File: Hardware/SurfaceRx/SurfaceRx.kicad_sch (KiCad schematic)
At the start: 26 parts

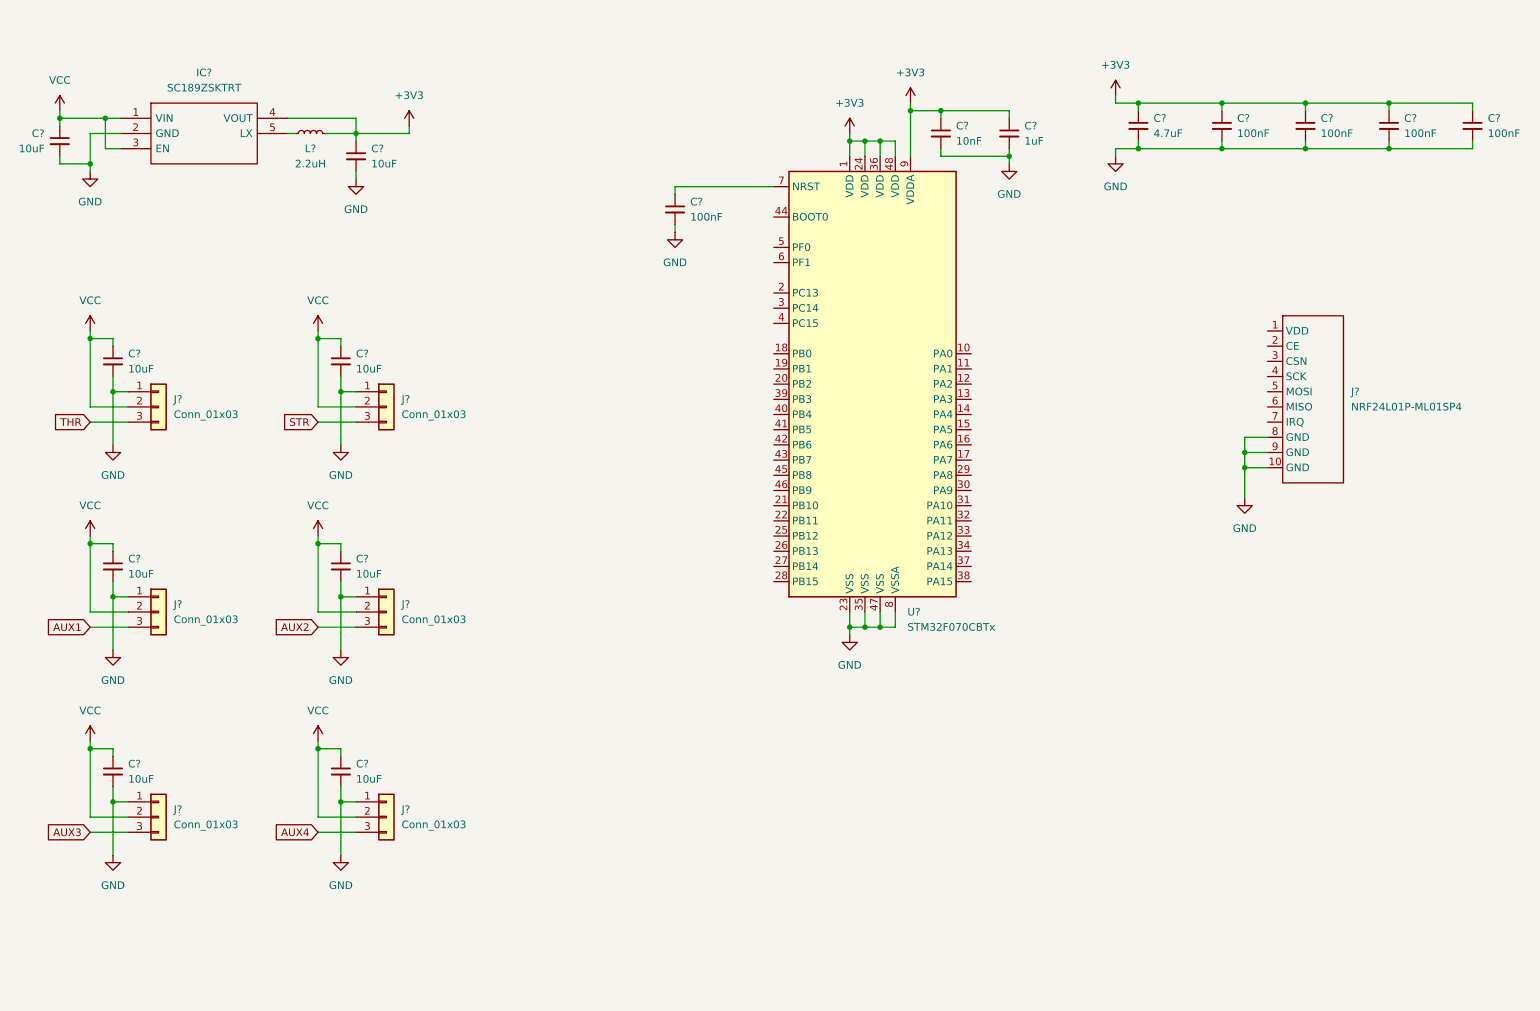
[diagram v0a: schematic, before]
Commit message: changed microcontroller to STM32G070KBT
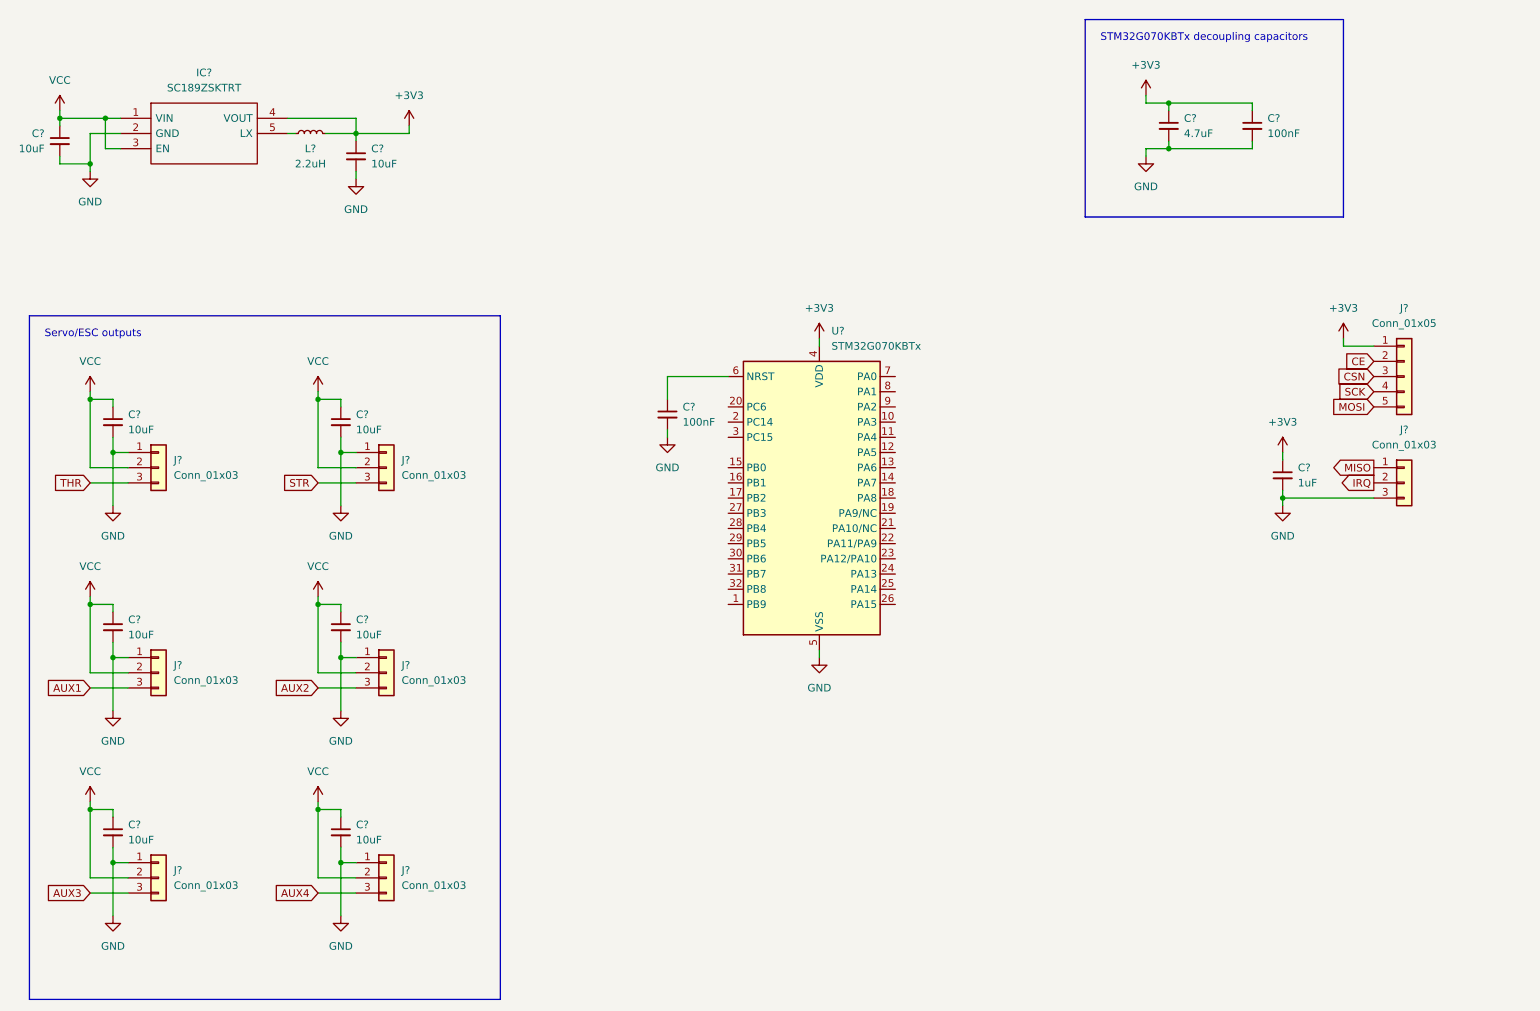
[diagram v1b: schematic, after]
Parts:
- removed C?: 10nF, symbol Device:C_Small
- removed C? (x3): 100nF, symbol Device:C_Small
- removed C?: 1uF, symbol Device:C_Small
- removed J?: NRF24L01P-ML01SP4, NRF24L01:ML01SP4, symbol NRF24L01:NRF24L01P-ML01SP4
- removed U?: STM32F070CBTx, Package_QFP:LQFP-48_7x7mm_P0.5mm, symbol MCU_ST_STM32F0:STM32F070CBTx
- added C?: 1uF, Capacitor_SMD:C_0603_1608Metric, symbol Device:C_Small
- added J?: Conn_01x05, Connector_PinHeader_2.54mm:PinHeader_1x05_P2.54mm_Vertical, symbol Connector_Generic:Conn_01x05
- added J?: Conn_01x03, Connector_PinHeader_2.54mm:PinHeader_1x03_P2.54mm_Vertical, symbol Connector_Generic:Conn_01x03
- added U?: STM32G070KBTx, Package_QFP:LQFP-32_7x7mm_P0.8mm, symbol MCU_ST_STM32G0:STM32G070KBTx
- C? (x11): footprint (none) -> Capacitor_SMD:C_0603_1608Metric
- L?: footprint (none) -> Custom_SurfaceRx:L-3.0x3.0mm; Part # (none) -> VLS3015CX-2R2M-H
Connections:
- net +3V3: now also C?.1, J?.1 (Pin_1), U?.4 (VDD)
- net GND: now also C?.2, J?.3 (Pin_3), U?.5 (VSS)
- net at C?.1: now also U?.6 (NRST)
- new net CE: J?.2 (Pin_2)
- new net CSN: J?.3 (Pin_3)
- new net IRQ: J?.2 (Pin_2)
- new net MISO: J?.1 (Pin_1)
- new net MOSI: J?.5 (Pin_5)
- new net SCK: J?.4 (Pin_4)
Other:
- note added: "STM32G070KBTx decoupling capacitors"
- note added: "Servo/ESC outputs"
- title: (none) -> SurfaceRx
- moved on the sheet: C?, J?

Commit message: added SWD and ESC (I2C) connectors. Connected NRF24 pins
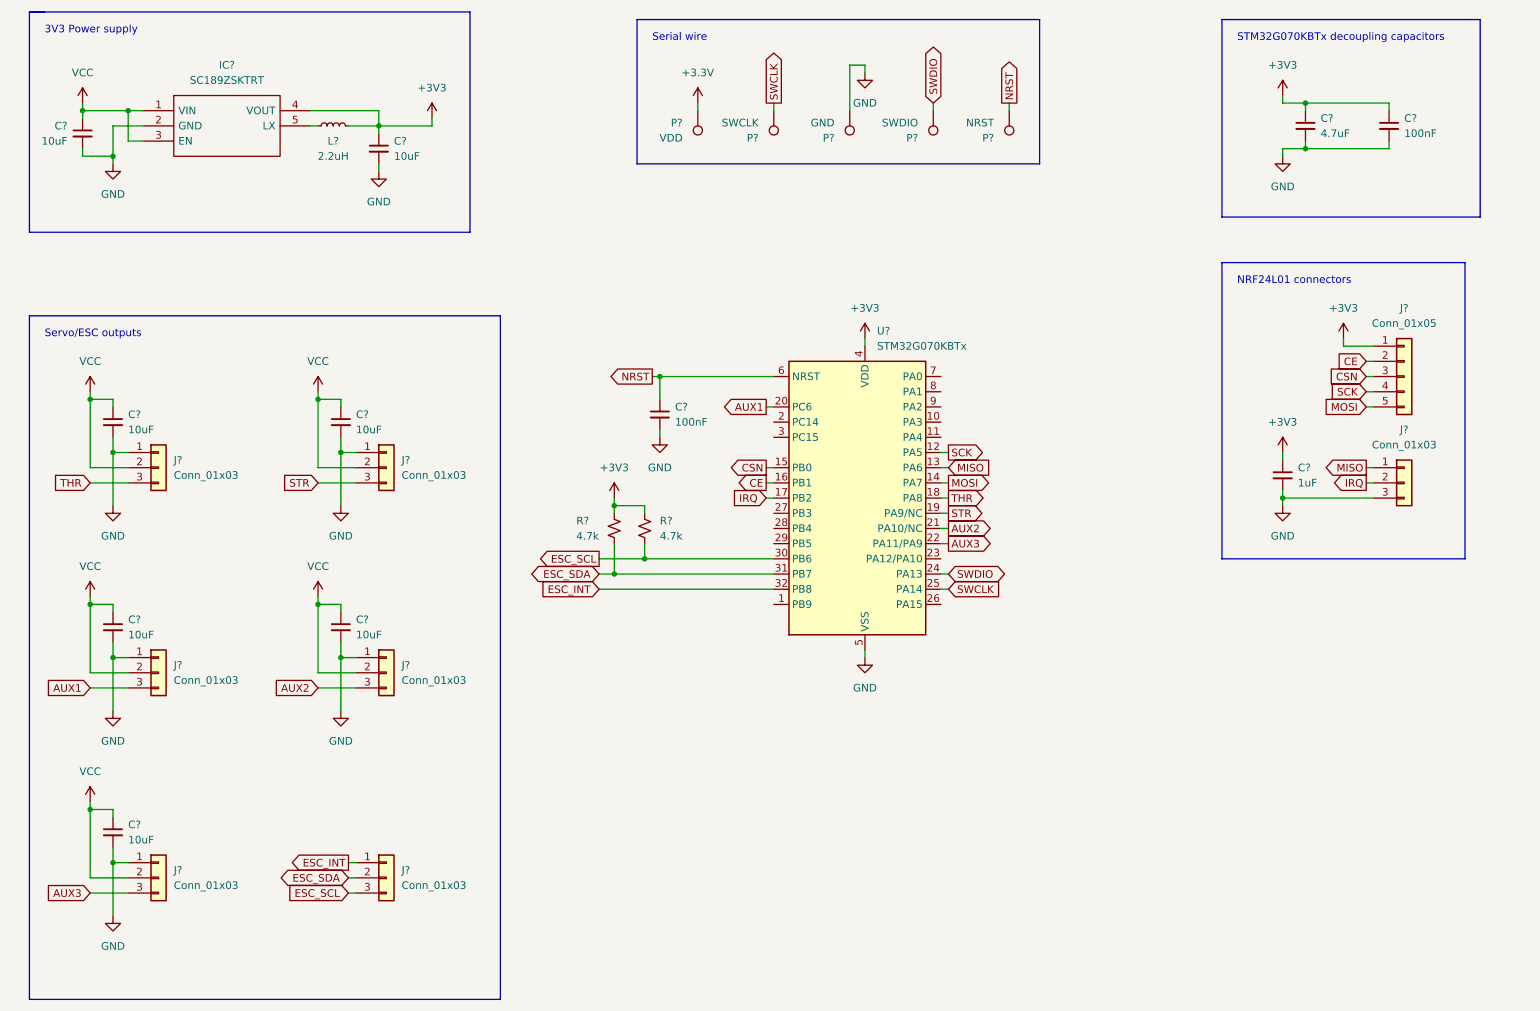
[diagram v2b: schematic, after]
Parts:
- removed C?: 10uF, Capacitor_SMD:C_0603_1608Metric, symbol Device:C_Small
- removed J?: Conn_01x03, Connector_PinHeader_1.27mm:PinHeader_1x03_P1.27mm_Vertical, symbol Connector_Generic:Conn_01x03
- added J?: Conn_01x03, Custom_SurfaceRx:JST-SH_3_Top, symbol Connector_Generic:Conn_01x03
- added P?: NRST, TestPoint:TestPoint_Pad_D1.5mm, symbol Connector:TestPoint
- added P?: SWCLK, TestPoint:TestPoint_Pad_D1.5mm, symbol Connector:TestPoint
- added P?: GND, TestPoint:TestPoint_Pad_D1.5mm, symbol Connector:TestPoint
- added P?: VDD, TestPoint:TestPoint_Pad_D1.5mm, symbol Connector:TestPoint
- added P?: SWDIO, TestPoint:TestPoint_Pad_D1.5mm, symbol Connector:TestPoint
- added R? (x2): 4.7k, Resistor_SMD:R_0603_1608Metric, symbol Device:R_Small_US
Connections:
- net +3V3: now also R?.1, R?.1
- net AUX1: now also U?.20 (PC6)
- net AUX2: now also U?.21 (PA10/NC)
- net AUX3: now also U?.22 (PA11/PA9)
- net CE: now also U?.16 (PB1)
- net CSN: now also U?.15 (PB0)
- net GND: now also P?.1
- net IRQ: now also U?.17 (PB2)
- net MISO: now also U?.13 (PA6)
- net MOSI: now also U?.14 (PA7)
- net SCK: now also U?.12 (PA5)
- net STR: now also U?.19 (PA9/NC)
- net THR: now also U?.18 (PA8)
- net SWDIO: now reaches U?.24 (PA13)
- net SWDIO: now also P?.1
- net SWCLK: now reaches U?.25 (PA14)
- net SWCLK: now also P?.1
- net ESC_SCL: now reaches U?.30 (PB6)
- net ESC_SCL: now also J?.3 (Pin_3), R?.2
- net ESC_SDA: now reaches U?.31 (PB7)
- net ESC_SDA: now also J?.2 (Pin_2), R?.2
- net ESC_INT: now reaches U?.32 (PB8)
- net ESC_INT: now also J?.1 (Pin_1)
- net NRST: now reaches C?.1, U?.6 (NRST)
- net NRST: now also P?.1
- new net +3.3V: P?.1
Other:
- note added: "3V3 Power supply"
- note added: "NRF24L01 connectors"
- note added: "Serial wire"
- moved on the sheet: C?, IC?, L?, U?

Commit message: annotated schematic
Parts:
- gave numbers to parts that had none: 29

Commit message: PCB partially layed out
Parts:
- J1, J2, J3, J4, J5: footprint Connector_PinHeader_1.27mm:PinHeader_1x03_P1.27mm_Vertical -> Connector_PinHeader_2.54mm:PinHeader_1x03_P2.54mm_Vertical
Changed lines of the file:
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@@
       (effects (font (size 1.27 1.27)) (justify left))
     )
-    (property "Footprint" "Connector_PinHeader_1.27mm:PinHeader_1x03_P1.27mm_Vertical" (id 2) (at 43.18 165.1 0)
+    (property "Footprint" "Connector_PinHeader_2.54mm:PinHeader_1x03_P2.54mm_Vertical" (id 2) (at 43.18 165.1 0)
       (effects (font (size 1.27 1.27)) hide)
     )
@@
       (effects (font (size 1.27 1.27)) (justify left))
     )
-    (property "Footprint" "Connector_PinHeader_1.27mm:PinHeader_1x03_P1.27mm_Vertical" (id 2) (at 81.28 130.81 0)
+    (property "Footprint" "Connector_PinHeader_2.54mm:PinHeader_1x03_P2.54mm_Vertical" (id 2) (at 81.28 130.81 0)
       (effects (font (size 1.27 1.27)) hide)
     )
@@
       (effects (font (size 1.27 1.27)) (justify left))
     )
-    (property "Footprint" "Connector_PinHeader_1.27mm:PinHeader_1x03_P1.27mm_Vertical" (id 2) (at 43.18 96.52 0)
+    (property "Footprint" "Connector_PinHeader_2.54mm:PinHeader_1x03_P2.54mm_Vertical" (id 2) (at 43.18 96.52 0)
       (effects (font (size 1.27 1.27)) hide)
     )
@@
       (effects (font (size 1.27 1.27)) (justify left))
     )
-    (property "Footprint" "Connector_PinHeader_1.27mm:PinHeader_1x03_P1.27mm_Vertical" (id 2) (at 43.18 130.81 0)
+    (property "Footprint" "Connector_PinHeader_2.54mm:PinHeader_1x03_P2.54mm_Vertical" (id 2) (at 43.18 130.81 0)
       (effects (font (size 1.27 1.27)) hide)
     )
@@
       (effects (font (size 1.27 1.27)) (justify left))
     )
-    (property "Footprint" "Connector_PinHeader_1.27mm:PinHeader_1x03_P1.27mm_Vertical" (id 2) (at 81.28 96.52 0)
+    (property "Footprint" "Connector_PinHeader_2.54mm:PinHeader_1x03_P2.54mm_Vertical" (id 2) (at 81.28 96.52 0)
       (effects (font (size 1.27 1.27)) hide)
     )
@@
     )
     (path "/6d28bcac-71e6-4094-bc46-8032e6c34cab"
-      (reference "J1") (unit 1) (value "Conn_01x03") (footprint "Connector_PinHeader_1.27mm:PinHeader_1x03_P1.27mm_Vertical")
+      (reference "J1") (unit 1) (value "Conn_01x03") (footprint "Connector_PinHeader_2.54mm:PinHeader_1x03_P2.54mm_Vertical")
     )
     (path "/cab3c3d3-a413-48ec-a811-423857c9ee91"
-      (reference "J2") (unit 1) (value "Conn_01x03") (footprint "Connector_PinHeader_1.27mm:PinHeader_1x03_P1.27mm_Vertical")
+      (reference "J2") (unit 1) (value "Conn_01x03") (footprint "Connector_PinHeader_2.54mm:PinHeader_1x03_P2.54mm_Vertical")
     )
     (path "/83dd7b31-f82d-4e59-aa13-cd3cdcd2e2d2"
-      (reference "J3") (unit 1) (value "Conn_01x03") (footprint "Connector_PinHeader_1.27mm:PinHeader_1x03_P1.27mm_Vertical")
+      (reference "J3") (unit 1) (value "Conn_01x03") (footprint "Connector_PinHeader_2.54mm:PinHeader_1x03_P2.54mm_Vertical")
     )
     (path "/6017f0ae-7b67-4ce4-b1c5-2e0b702a2107"
-      (reference "J4") (unit 1) (value "Conn_01x03") (footprint "Connector_PinHeader_1.27mm:PinHeader_1x03_P1.27mm_Vertical")
+      (reference "J4") (unit 1) (value "Conn_01x03") (footprint "Connector_PinHeader_2.54mm:PinHeader_1x03_P2.54mm_Vertical")
     )
     (path "/20644983-0b46-406b-8b20-b0c47ec274a1"
-      (reference "J5") (unit 1) (value "Conn_01x03") (footprint "Connector_PinHeader_1.27mm:PinHeader_1x03_P1.27mm_Vertical")
+      (reference "J5") (unit 1) (value "Conn_01x03") (footprint "Connector_PinHeader_2.54mm:PinHeader_1x03_P2.54mm_Vertical")
     )
     (path "/0e4575fc-3bef-4d0b-82d7-c038a561294a"
